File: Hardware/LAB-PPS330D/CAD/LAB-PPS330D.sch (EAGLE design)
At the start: 8 parts, among them J1 100mil, J2 100mil, U1 SN74LVC1G139, U2 ADP1196, U3 ADP1196, U4 ADP1196, U5 ADP1196, U6 SN74LVC3G04DCURBGA

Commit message: 1) This is the final Rev1 version going off to MFG
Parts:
- removed U5: ADP1196, My Library-adm:ADP1196
- removed U6: SN74LVC3G04DCURBGA, My Library-adm:SN74LVC3G04DCURBGA
- added R1: 1K, SparkFun-Resistors:1KOHM-1/10W-1%(0603)
- added V0, V1, V2: RED, SparkFun-LED:LED-RED0603
- U1: value SN74LVC1G139 -> SN74LVC1G139DCU; device My Library-adm:SN74LVC1G139 -> LAB-PPS330D:SN74LVC1G139DCU
- U2: value ADP1196 -> FDC6420C; device My Library-adm:ADP1196 -> LAB-PPS330D:FDC6420C
- U3, U4: value ADP1196 -> FDC6312P; device My Library-adm:ADP1196 -> LAB-PPS330D:FDC6312P
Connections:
- removed net N$3: U4.EN, U6.3Y
- removed net N$4: U1.Y0, U6.1A
- removed net N$6: U1.Y2, U6.3A
- removed net N$7: U1.Y3, U5.EN
- new net GNDS: U1.Y3, U2N.G
- new net V0S: U1.Y0, U2P.G, V0.C
- new net V1S: U1.Y1, U3A.G, U3B.G, V1.C
- new net V2S: U1.Y2, U4A.G, U4B.G, V2.C
- net DGND: now also U2N.S; no longer U5.VIN
- net N$1: now also U3A.D, U3B.D; no longer U2.EN, U6.1Y
- net N$2: now also U4A.D, U4B.D; no longer U3.EN, U6.2Y
- net N$5: now also R1.2, V0.A, V1.A, V2.A; no longer U1.Y1, U6.2A
- net PE: now also U2N.D; no longer U2.GND, U3.GND, U4.GND, U5.GND, U5.VOUT, U6.GND
- net S0: now also J2.1; no longer J2.3
- net V0: now also R1.1, U2P.S; no longer U2.VIN, U6.VCC
- net V1: now also U3A.S; no longer U3.VIN
- net V2: now also U4A.S; no longer U4.VIN
- net VOUT: now also J2.3, U2P.D, U3B.S, U4B.S; no longer J2.1, U2.VOUT, U3.VOUT, U4.VOUT
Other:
- note removed: "SN74LVC1G139"
- note removed: "U1"
- moved on the sheet: J1, J2

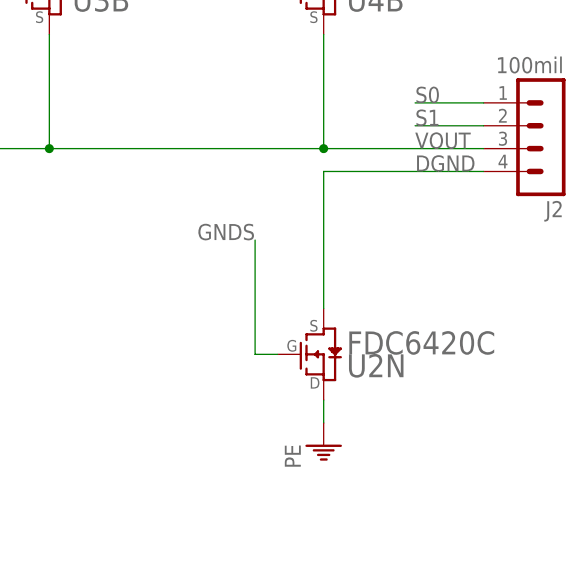
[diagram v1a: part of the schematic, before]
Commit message: 1) Fixing the symbol / device for the FDC6420C MOSFET in the library. The symbol had the source/drain marked incorrectly though the device was pinned out correctly. 2) Because the symbol was wrong, I connected it wrong on the schematic ... So I fixed that 3) Then I fixed the layout to adjust for it. 4) Fixed the silkscreen had the signals on the bottom layer wrong. 5) Also adjusted the simulation to work correctly ... with the source and drain in the proper location for a low-side switch.
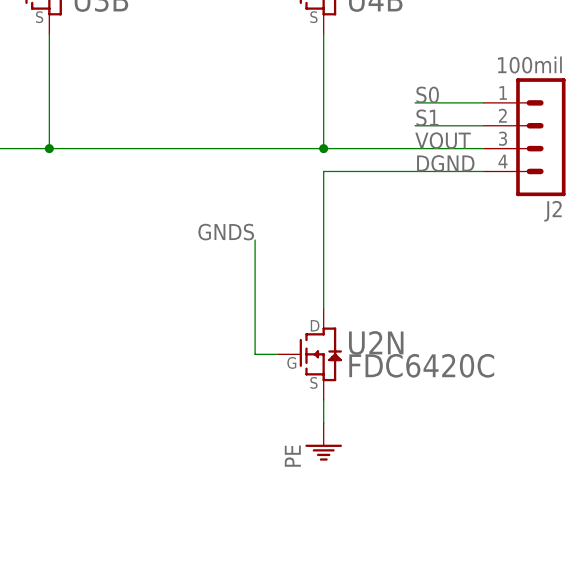
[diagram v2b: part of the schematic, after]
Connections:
- net DGND: now also U2N.D; no longer U2N.S
- net PE: now also U2N.S; no longer U2N.D
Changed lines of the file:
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@@
 <?xml version="1.0" encoding="utf-8"?>
 <!DOCTYPE eagle SYSTEM "eagle.dtd">
-<eagle version="6.6.0">
+<eagle version="6.5.0">
 <drawing>
 <settings>
@@
 <segment>
 <pinref part="PE1" gate="M" pin="PE"/>
-<pinref part="U2" gate="N" pin="D"/>
+<pinref part="U2" gate="N" pin="S"/>
 <wire x1="215.9" y1="66.04" x2="215.9" y2="68.58" width="0.1524" layer="91"/>
 </segment>
@@
 <wire x1="233.68" y1="93.98" x2="215.9" y2="93.98" width="0.1524" layer="91"/>
 <label x="226.06" y="93.98" size="1.778" layer="95"/>
-<pinref part="U2" gate="N" pin="S"/>
-<wire x1="215.9" y1="93.98" x2="215.9" y2="78.74" width="0.1524" layer="91"/>
-</segment>
-</net>
+<pinref part="U2" gate="N" pin="D"/>
+<wire x1="215.9" y1="78.74" x2="215.9" y2="93.98" width="0.1524" layer="91"/>
+</segment>
+</net>

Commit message: 1) Fixing the pinout on the PPS330D to match what is on the DEB429A -- the select lines are still off though. 2) Updating the BOM for the PLR5010D -- adding the base resistor for the BJTs
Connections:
- net S0: now also J2.2; no longer J2.1
- net S1: now also J2.3; no longer J2.2
- net VOUT: now also J2.1; no longer J2.3
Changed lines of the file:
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@@
 <?xml version="1.0" encoding="utf-8"?>
 <!DOCTYPE eagle SYSTEM "eagle.dtd">
-<eagle version="6.5.0">
+<eagle version="6.6.0">
 <drawing>
 <settings>
@@
 </segment>
 <segment>
-<wire x1="233.68" y1="101.6" x2="226.06" y2="101.6" width="0.1524" layer="91"/>
-<pinref part="J2" gate="1" pin="1"/>
-<label x="226.06" y="101.6" size="1.778" layer="95"/>
+<wire x1="233.68" y1="99.06" x2="226.06" y2="99.06" width="0.1524" layer="91"/>
+<label x="226.06" y="99.06" size="1.778" layer="95"/>
+<pinref part="J2" gate="1" pin="2"/>
 </segment>
 </net>
@@
 </segment>
 <segment>
-<wire x1="233.68" y1="99.06" x2="226.06" y2="99.06" width="0.1524" layer="91"/>
-<pinref part="J2" gate="1" pin="2"/>
-<label x="226.06" y="99.06" size="1.778" layer="95"/>
+<wire x1="233.68" y1="96.52" x2="226.06" y2="96.52" width="0.1524" layer="91"/>
+<label x="226.06" y="96.52" size="1.778" layer="95"/>
+<pinref part="J2" gate="1" pin="3"/>
 </segment>
 </net>
@@
 <net name="VOUT" class="0">
 <segment>
-<wire x1="215.9" y1="109.22" x2="215.9" y2="96.52" width="0.1524" layer="91"/>
-<wire x1="185.42" y1="109.22" x2="185.42" y2="96.52" width="0.1524" layer="91"/>
-<wire x1="185.42" y1="96.52" x2="215.9" y2="96.52" width="0.1524" layer="91"/>
-<wire x1="185.42" y1="96.52" x2="154.94" y2="96.52" width="0.1524" layer="91"/>
-<wire x1="154.94" y1="96.52" x2="154.94" y2="109.22" width="0.1524" layer="91"/>
-<junction x="185.42" y="96.52"/>
-<pinref part="J2" gate="1" pin="3"/>
-<wire x1="233.68" y1="96.52" x2="215.9" y2="96.52" width="0.1524" layer="91"/>
-<junction x="215.9" y="96.52"/>
-<label x="226.06" y="96.52" size="1.778" layer="95"/>
+<wire x1="215.9" y1="109.22" x2="215.9" y2="101.6" width="0.1524" layer="91"/>
+<wire x1="185.42" y1="109.22" x2="185.42" y2="101.6" width="0.1524" layer="91"/>
+<wire x1="185.42" y1="101.6" x2="215.9" y2="101.6" width="0.1524" layer="91"/>
+<wire x1="185.42" y1="101.6" x2="154.94" y2="101.6" width="0.1524" layer="91"/>
+<wire x1="154.94" y1="101.6" x2="154.94" y2="109.22" width="0.1524" layer="91"/>
+<junction x="185.42" y="101.6"/>
 <pinref part="U2" gate="P" pin="D"/>
 <pinref part="U3" gate="B" pin="S"/>
 <pinref part="U4" gate="B" pin="S"/>
-</segment>
-</net>
+<wire x1="233.68" y1="101.6" x2="215.9" y2="101.6" width="0.1524" layer="91"/>
+<label x="226.06" y="101.6" size="1.778" layer="95"/>
+<pinref part="J2" gate="1" pin="1"/>
+<junction x="215.9" y="101.6"/>
+</segment>
+</net>

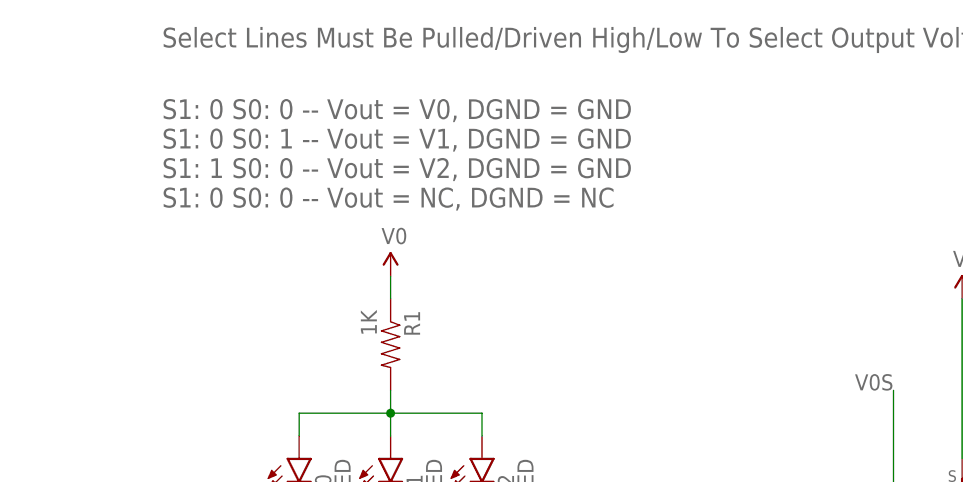
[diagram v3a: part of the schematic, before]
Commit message: 1) Correcting the usage description on the schematic
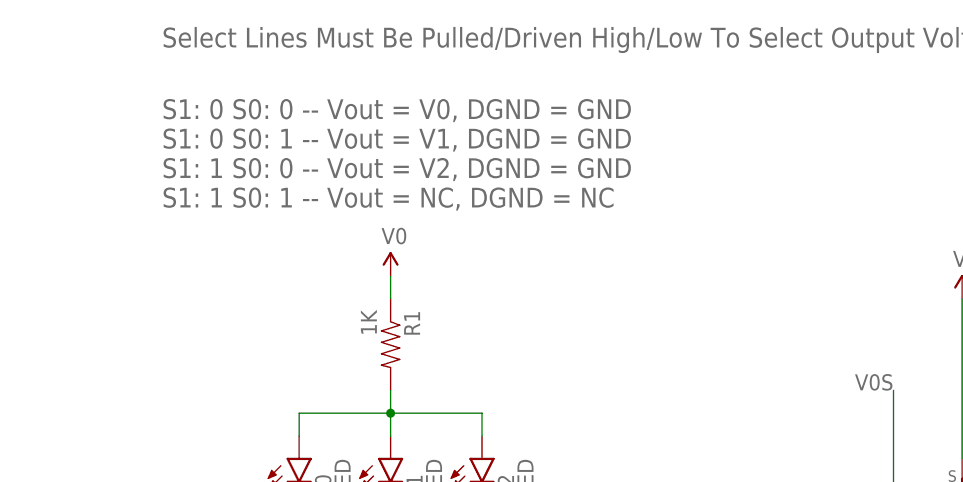
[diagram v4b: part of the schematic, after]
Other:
- note added: "S1: 0 S0: 0 -- Vout = V0, DGND = GND S1: 0 S0: 1 -- Vout = V1, DGND = GND S1: 1 S0: 0 -- Vout = V2, DGND = GND S1: 1 S0: 1 -- Vout = NC, DGND = NC"
- note removed: "S1: 0 S0: 0 -- Vout = V0, DGND = GND S1: 0 S0: 1 -- Vout = V1, DGND = GND S1: 1 S0: 0 -- Vout = V2, DGND = GND S1: 0 S0: 0 -- Vout = NC, DGND = NC"
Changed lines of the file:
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@@
 <text x="241.3" y="7.62" size="2.54" layer="94" rot="MR0">0</text>
 <text x="170.18" y="25.4" size="6.4516" layer="94">LAB304  LLC.</text>
-<text x="66.04" y="165.1" size="2.1844" layer="95">Select Lines Must Be Pulled/Driven High/Low To Select Output Voltage</text>
-<text x="66.04" y="147.32" size="2.1844" layer="95">S1: 0 S0: 0 -- Vout = V0, DGND = GND
+<text x="66.04" y="165.1" size="2.1844" layer="95" font="vector">Select Lines Must Be Pulled/Driven High/Low To Select Output Voltage</text>
+<text x="66.04" y="147.32" size="2.1844" layer="95" font="vector">S1: 0 S0: 0 -- Vout = V0, DGND = GND
 S1: 0 S0: 1 -- Vout = V1, DGND = GND
 S1: 1 S0: 0 -- Vout = V2, DGND = GND
-S1: 0 S0: 0 -- Vout = NC, DGND = NC
+S1: 1 S0: 1 -- Vout = NC, DGND = NC
 </text>
 </plain>
